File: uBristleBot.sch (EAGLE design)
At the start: 32 parts, among them M1 MOTOR-304-103, M2 MOTOR-304-103, Q1 2N7002BKV, U2 MCP7383X.DFN, U3 LM3668, U4 TPS727XX.DSE

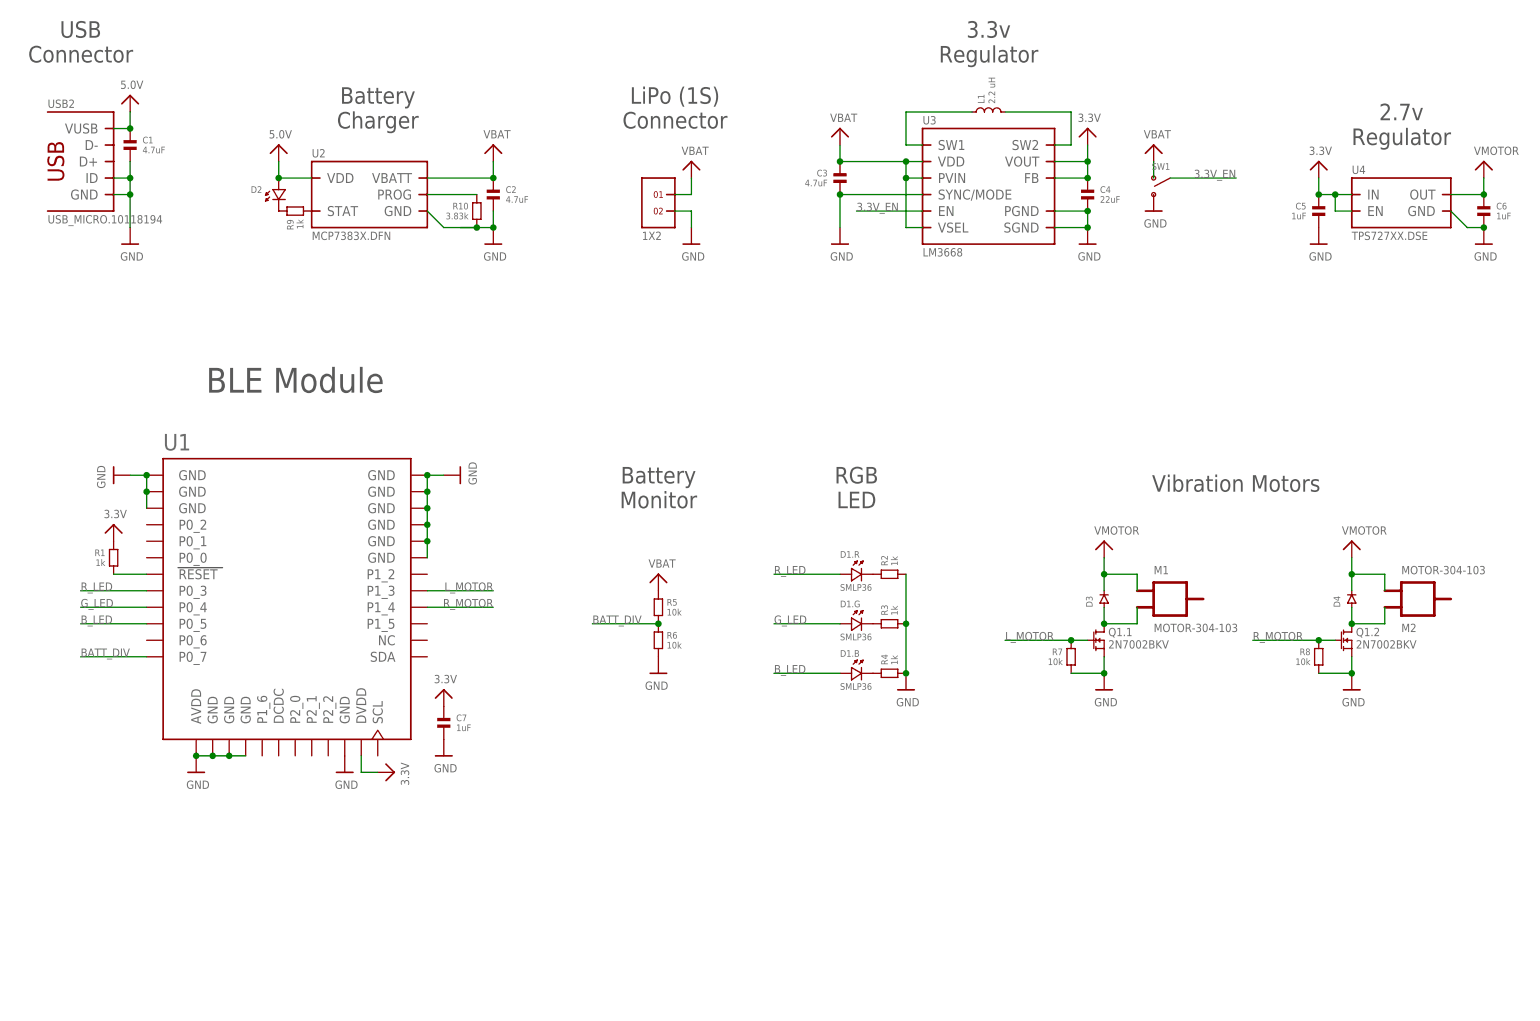
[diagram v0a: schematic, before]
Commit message: Component placement mostly complete. Beginning layout
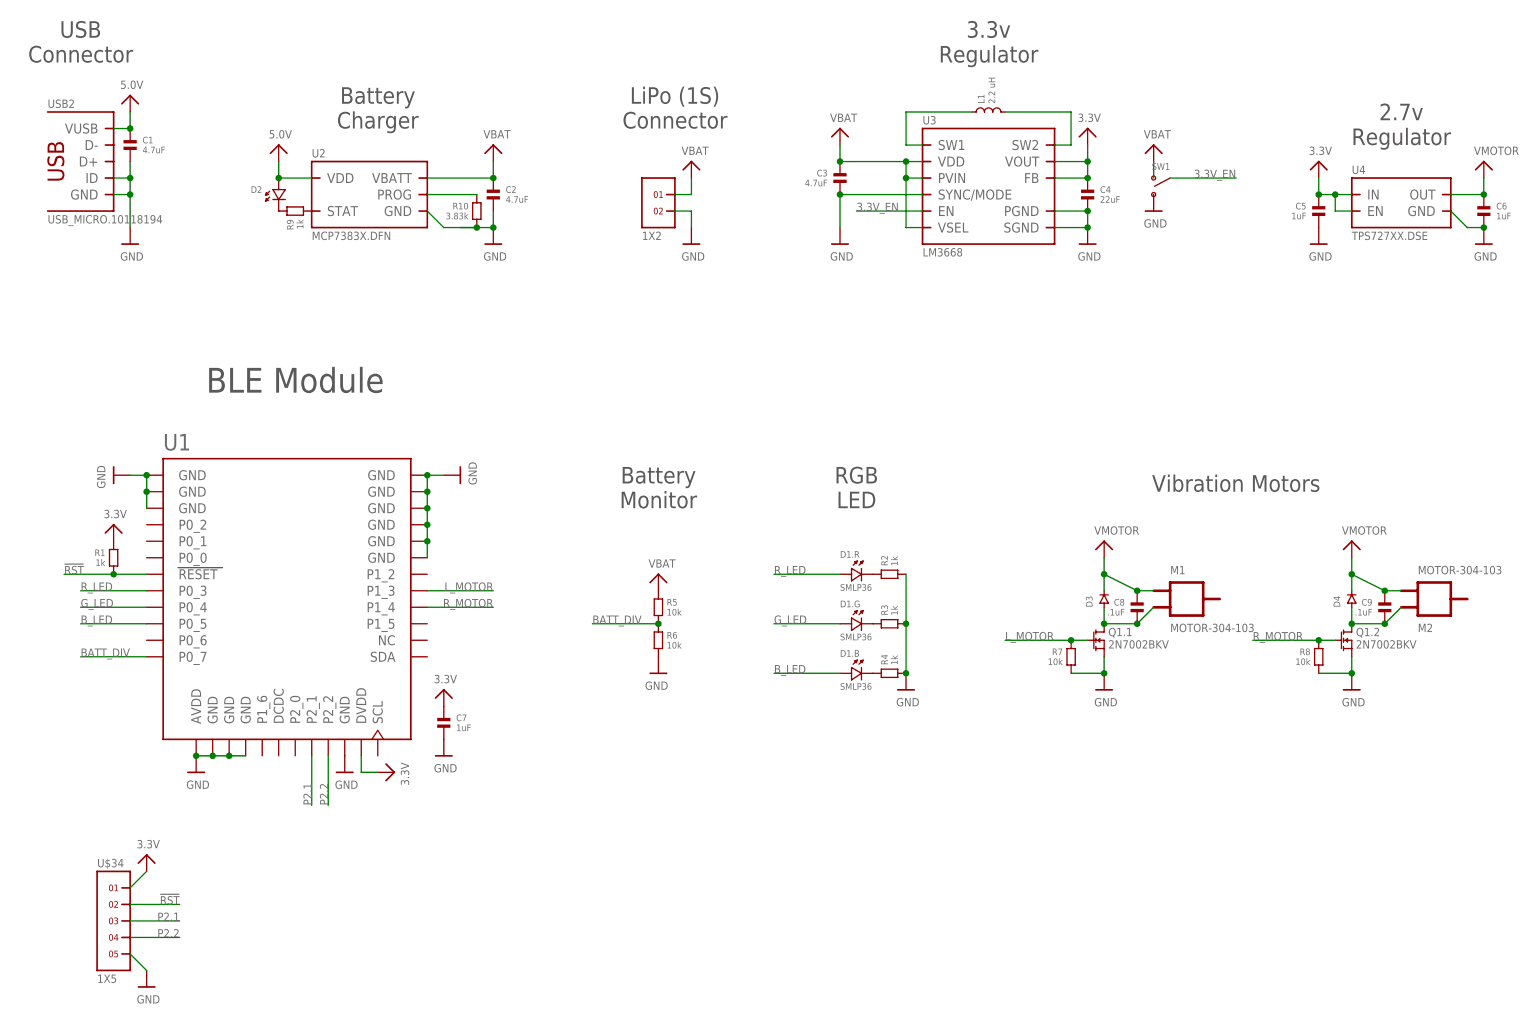
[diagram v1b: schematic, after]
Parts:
- added C8, C9: .1uF, standardparts:CAPACITOR.0402
- added U$34: 1X5, headers(2mm):1X5
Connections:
- removed net N$7: R1.2, U1.RESET
- new net !RST: R1.2, U$34.2, U1.RESET
- new net P2.1: U$34.3, U1.P2_1
- new net P2.2: U$34.4, U1.P2_2
- net 3.3V: now also U$34.1
- net GND: now also U$34.5
- net N$6: now also C8.2
- net N$8: now also C9.2
- net VMOTOR: now also C8.1, C9.1
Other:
- moved on the sheet: M1, M2

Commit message: Layout complete and ready for review
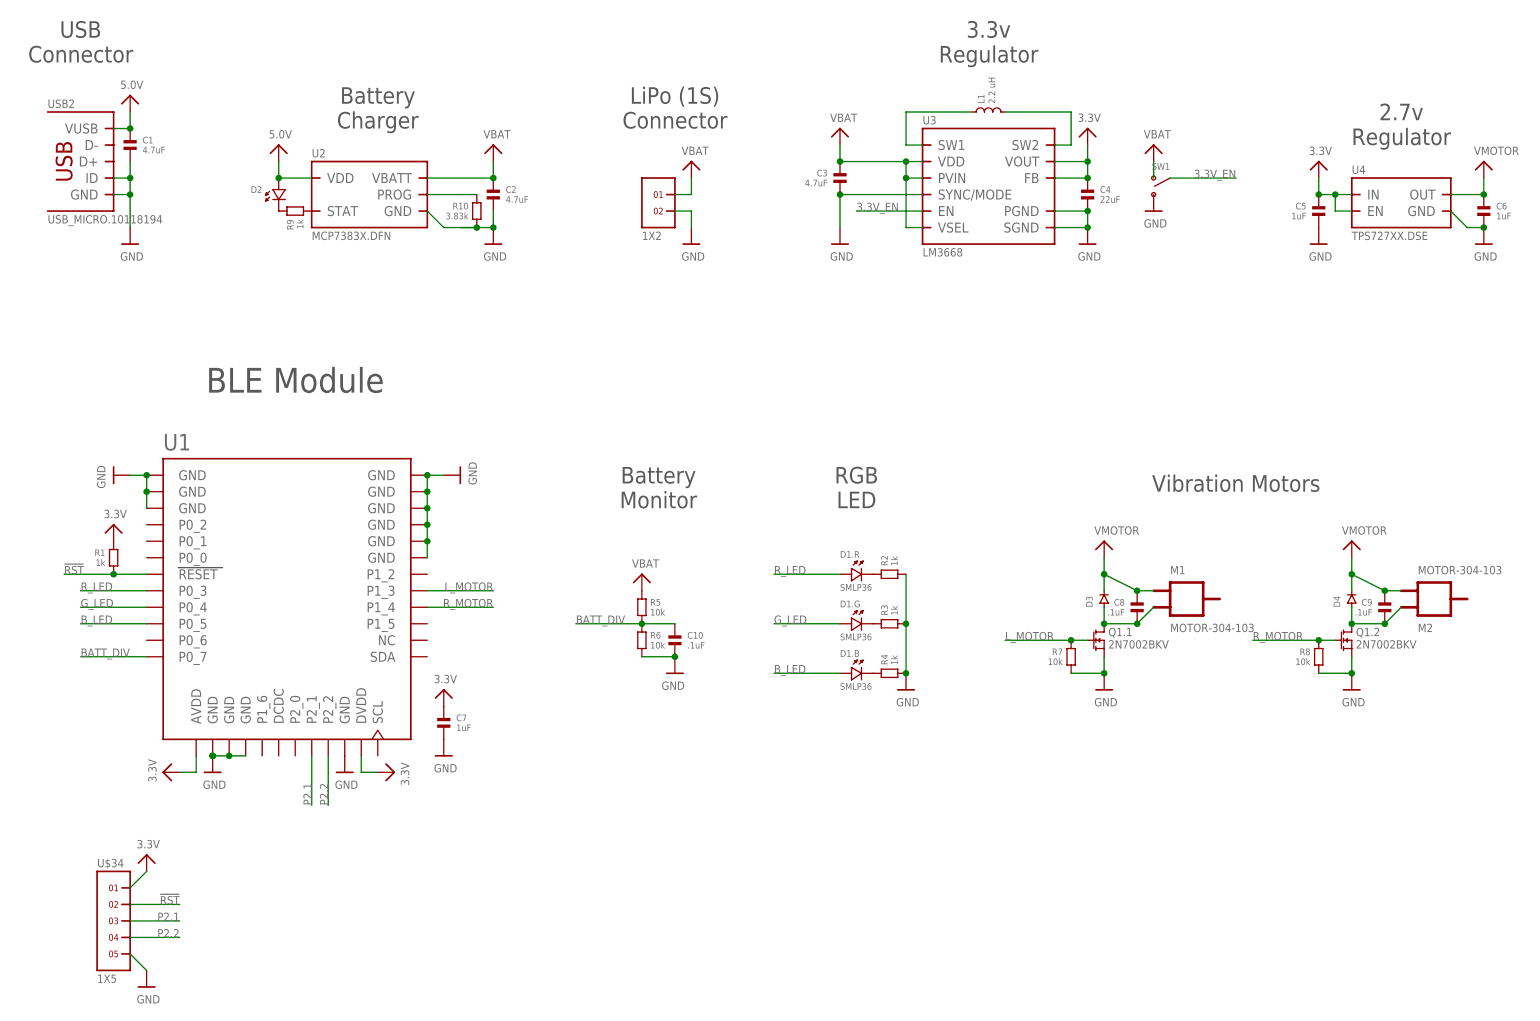
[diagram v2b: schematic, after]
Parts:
- added C10: .1uF, standardparts:CAPACITOR.0402
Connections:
- net 3.3V: now also U1.AVDD
- net BATT_DIV: now also C10.1
- net GND: now also C10.2; no longer U1.AVDD
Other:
- moved on the sheet: R5, R6, USB2
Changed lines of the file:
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@@
 <grid distance="0.1" unitdist="inch" unit="inch" style="lines" multiple="1" display="no" altdistance="0.01" altunitdist="inch" altunit="inch"/>
 <layers>
-<layer number="1" name="Top" color="4" fill="1" visible="no" active="no"/>
-<layer number="16" name="Bottom" color="1" fill="1" visible="no" active="no"/>
-<layer number="17" name="Pads" color="2" fill="1" visible="no" active="no"/>
-<layer number="18" name="Vias" color="2" fill="1" visible="no" active="no"/>
-<layer number="19" name="Unrouted" color="6" fill="1" visible="no" active="no"/>
-<layer number="20" name="Dimension" color="15" fill="1" visible="no" active="no"/>
-<layer number="21" name="tPlace" color="7" fill="1" visible="no" active="no"/>
-<layer number="22" name="bPlace" color="7" fill="1" visible="no" active="no"/>
-<layer number="23" name="tOrigins" color="15" fill="1" visible="no" active="no"/>
-<layer number="24" name="bOrigins" color="15" fill="1" visible="no" active="no"/>
-<layer number="25" name="tNames" color="7" fill="1" visible="no" active="no"/>
-<layer number="26" name="bNames" color="7" fill="1" visible="no" active="no"/>
-<layer number="27" name="tValues" color="7" fill="1" visible="no" active="no"/>
-<layer number="28" name="bValues" color="7" fill="1" visible="no" active="no"/>
+<layer number="1" name="Top" color="4" fill="1" visible="yes" active="no"/>
+<layer number="16" name="Bottom" color="1" fill="1" visible="yes" active="no"/>
+<layer number="17" name="Pads" color="2" fill="1" visible="yes" active="no"/>
+<layer number="18" name="Vias" color="2" fill="1" visible="yes" active="no"/>
+<layer number="19" name="Unrouted" color="6" fill="1" visible="yes" active="no"/>
+<layer number="20" name="Dimension" color="15" fill="1" visible="yes" active="no"/>
+<layer number="21" name="tPlace" color="7" fill="1" visible="yes" active="no"/>
+<layer number="22" name="bPlace" color="7" fill="1" visible="yes" active="no"/>
+<layer number="23" name="tOrigins" color="15" fill="1" visible="yes" active="no"/>
+<layer number="24" name="bOrigins" color="15" fill="1" visible="yes" active="no"/>
+<layer number="25" name="tNames" color="7" fill="1" visible="yes" active="no"/>
+<layer number="26" name="bNames" color="7" fill="1" visible="yes" active="no"/>
+<layer number="27" name="tValues" color="7" fill="1" visible="yes" active="no"/>
+<layer number="28" name="bValues" color="7" fill="1" visible="yes" active="no"/>
 <layer number="29" name="tStop" color="7" fill="3" visible="no" active="no"/>
 <layer number="30" name="bStop" color="7" fill="6" visible="no" active="no"/>
@@
 <layer number="35" name="tGlue" color="7" fill="4" visible="no" active="no"/>
 <layer number="36" name="bGlue" color="7" fill="5" visible="no" active="no"/>
-<layer number="37" name="tTest" color="7" fill="1" visible="no" active="no"/>
-<layer number="38" name="bTest" color="7" fill="1" visible="no" active="no"/>
+<layer number="37" name="tTest" color="7" fill="1" visible="yes" active="no"/>
+<layer number="38" name="bTest" color="7" fill="1" visible="yes" active="no"/>
 <layer number="39" name="tKeepout" color="4" fill="11" visible="no" active="no"/>
 <layer number="40" name="bKeepout" color="1" fill="11" visible="no" active="no"/>
@@
 <layer number="44" name="Drills" color="7" fill="1" visible="no" active="no"/>
 <layer number="45" name="Holes" color="7" fill="1" visible="no" active="no"/>
-<layer number="46" name="Milling" color="3" fill="1" visible="no" active="no"/>
-<layer number="47" name="Measures" color="7" fill="1" visible="no" active="no"/>
-<layer number="48" name="Document" color="7" fill="1" visible="no" active="no"/>
-<layer number="49" name="Reference" color="7" fill="1" visible="no" active="no"/>
-<layer number="50" name="dxf" color="7" fill="1" visible="no" active="no"/>
-<layer number="51" name="tDocu" color="7" fill="1" visible="no" active="no"/>
-<layer number="52" name="bDocu" color="7" fill="1" visible="no" active="no"/>
-<layer number="53" name="tGND_GNDA" color="7" fill="9" visible="no" active="no"/>
-<layer number="54" name="bGND_GNDA" color="1" fill="9" visible="no" active="no"/>
-<layer number="56" name="wert" color="7" fill="1" visible="no" active="no"/>
-<layer number="59" name="Invisible" color="7" fill="1" visible="no" active="no"/>
-<layer number="61" name="stand" color="7" fill="1" visible="no" active="no"/>
+<layer number="46" name="Milling" color="3" fill="1" visible="yes" active="no"/>
+<layer number="47" name="Measures" color="7" fill="1" visible="yes" active="no"/>
+<layer number="48" name="Document" color="7" fill="1" visible="yes" active="no"/>
+<layer number="49" name="Reference" color="7" fill="1" visible="yes" active="no"/>
+<layer number="50" name="dxf" color="7" fill="1" visible="yes" active="no"/>
+<layer number="51" name="tDocu" color="7" fill="1" visible="yes" active="no"/>
+<layer number="52" name="bDocu" color="7" fill="1" visible="yes" active="no"/>
+<layer number="53" name="tGND_GNDA" color="7" fill="9" visible="yes" active="no"/>
+<layer number="54" name="bGND_GNDA" color="1" fill="9" visible="yes" active="no"/>
+<layer number="56" name="wert" color="7" fill="1" visible="yes" active="no"/>
+<layer number="59" name="Invisible" color="7" fill="1" visible="yes" active="no"/>
+<layer number="61" name="stand" color="7" fill="1" visible="yes" active="no"/>
 <layer number="90" name="Modules" color="5" fill="1" visible="yes" active="yes"/>
 <layer number="91" name="Nets" color="2" fill="1" visible="yes" active="yes"/>
@@
 <part name="U$35" library="microbuilder" deviceset="GND" device=""/>
 <part name="U$36" library="microbuilder" deviceset="3.3V" device=""/>
+<part name="C10" library="standardparts" deviceset="CAPACITOR" device=".0402" value=".1uF"/>
+<part name="U$37" library="microbuilder" deviceset="3.3V" device=""/>
 </parts>
 <sheets>
@@
 <instance part="U$2" gate="G$1" x="30.48" y="91.44" rot="R270"/>
 <instance part="U$3" gate="G$1" x="33.02" y="127"/>
-<instance part="U$4" gate="G$1" x="43.18" y="45.72"/>
+<instance part="U$4" gate="G$1" x="45.72" y="45.72"/>
 <instance part="U$5" gate="G$1" x="66.04" y="45.72"/>
 <instance part="U2" gate="G$1" x="68.58" y="134.62"/>
@@
 <instance part="R3" gate="G$1" x="149.86" y="68.58"/>
 <instance part="R4" gate="G$1" x="149.86" y="60.96"/>
-<instance part="R5" gate="G$1" x="114.3" y="71.12" rot="R270"/>
-<instance part="R6" gate="G$1" x="114.3" y="66.04" rot="R270"/>
+<instance part="R5" gate="G$1" x="111.76" y="71.12" rot="R270"/>
+<instance part="R6" gate="G$1" x="111.76" y="66.04" rot="R270"/>
 <instance part="R7" gate="G$1" x="177.8" y="63.5" rot="MR270"/>
 <instance part="R8" gate="G$1" x="215.9" y="63.5" rot="MR270"/>
 <instance part="U$13" gate="G$1" x="152.4" y="58.42"/>
 <instance part="U$14" gate="G$1" x="30.48" y="83.82"/>
-<instance part="U$16" gate="G$1" x="114.3" y="60.96" rot="MR0"/>
+<instance part="U$16" gate="G$1" x="116.84" y="60.96" rot="MR0"/>
 <instance part="U$17" gate="G$1" x="215.9" y="139.7"/>
 <instance part="U$19" gate="G$1" x="73.66" y="45.72" rot="R270"/>
-<instance part="U$15" gate="G$1" x="114.3" y="76.2"/>
+<instance part="U$15" gate="G$1" x="111.76" y="76.2"/>
 <instance part="C1" gate="G$1" x="33.02" y="142.24" rot="R270"/>
 <instance part="D2" gate="G$1" x="55.88" y="134.62" rot="MR270"/>
@@
 <instance part="U$35" gate="G$1" x="35.56" y="12.7"/>
 <instance part="U$36" gate="G$1" x="35.56" y="33.02"/>
+<instance part="C10" gate="G$1" x="116.84" y="66.04" rot="R270"/>
+<instance part="U$37" gate="G$1" x="38.1" y="45.72" rot="R90"/>
 </instances>
 <busses>
@@
 <segment>
 <pinref part="U1" gate="G$1" pin="GND@6"/>
-<pinref part="U1" gate="G$1" pin="AVDD"/>
 <wire x1="50.8" y1="48.26" x2="48.26" y2="48.26" width="0.1524" layer="91"/>
 <pinref part="U$4" gate="G$1" pin="GND"/>
 <wire x1="48.26" y1="48.26" x2="45.72" y2="48.26" width="0.1524" layer="91"/>
-<wire x1="45.72" y1="48.26" x2="43.18" y2="48.26" width="0.1524" layer="91"/>
-<junction x="43.18" y="48.26"/>
+<junction x="45.72" y="48.26"/>
 <pinref part="U1" gate="G$1" pin="GND@4"/>
 <junction x="45.72" y="48.26"/>
@@
 <wire x1="152.4" y1="68.58" x2="152.4" y2="76.2" width="0.1524" layer="91"/>
 <junction x="152.4" y="68.58"/>
-</segment>
-<segment>
-<pinref part="R6" gate="G$1" pin="2"/>
-<pinref part="U$16" gate="G$1" pin="GND"/>
 </segment>
 <segment>
@@
 <wire x1="35.56" y1="15.24" x2="33.02" y2="17.78" width="0.1524" layer="91"/>
 </segment>
+<segment>
+<pinref part="C10" gate="G$1" pin="2"/>
+<pinref part="U$16" gate="G$1" pin="GND"/>
+<pinref part="R6" gate="G$1" pin="2"/>
+<wire x1="111.76" y1="63.5" x2="116.84" y2="63.5" width="0.1524" layer="91"/>
+<junction x="116.84" y="63.5"/>
+</segment>
 </net>
 <net name="5.0V" class="0">
@@
 <wire x1="33.02" y1="27.94" x2="35.56" y2="30.48" width="0.1524" layer="91"/>
 </segment>
+<segment>
+<pinref part="U$37" gate="G$1" pin="3.3V"/>
+<pinref part="U1" gate="G$1" pin="AVDD"/>
+<wire x1="40.64" y1="45.72" x2="43.18" y2="45.72" width="0.1524" layer="91"/>
+<wire x1="43.18" y1="45.72" x2="43.18" y2="48.26" width="0.1524" layer="91"/>
+</segment>
 </net>
 <net name="N$2" class="0">
@@
 <pinref part="R5" gate="G$1" pin="2"/>
 <pinref part="R6" gate="G$1" pin="1"/>
-<wire x1="114.3" y1="68.58" x2="104.14" y2="68.58" width="0.1524" layer="91"/>
-<junction x="114.3" y="68.58"/>
-<label x="104.14" y="68.58" size="1.27" layer="95"/>
-</segment>
-</net>
+<wire x1="111.76" y1="68.58" x2="101.6" y2="68.58" width="0.1524" layer="91"/>
+<junction x="111.76" y="68.58"/>
+<label x="101.6" y="68.58" size="1.27" layer="95"/>
+<pinref part="C10" gate="G$1" pin="1"/>
+<wire x1="116.84" y1="68.58" x2="111.76" y2="68.58" width="0.1524" layer="91"/>
+</segment>
+</net>
